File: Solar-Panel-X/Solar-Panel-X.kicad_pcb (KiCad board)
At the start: 6 copper layers, 48.4 x 48.4 mm, 81 parts, among them J1 FTS-105-01-L-DV-A, Q1 BSS138DWQ-7, Q2 MBT2222ADW1T1, Q3 BSS138DWQ-7, Q4 MBT2222ADW1T1, U1 BQ25570RGRR, U2 TSL2561

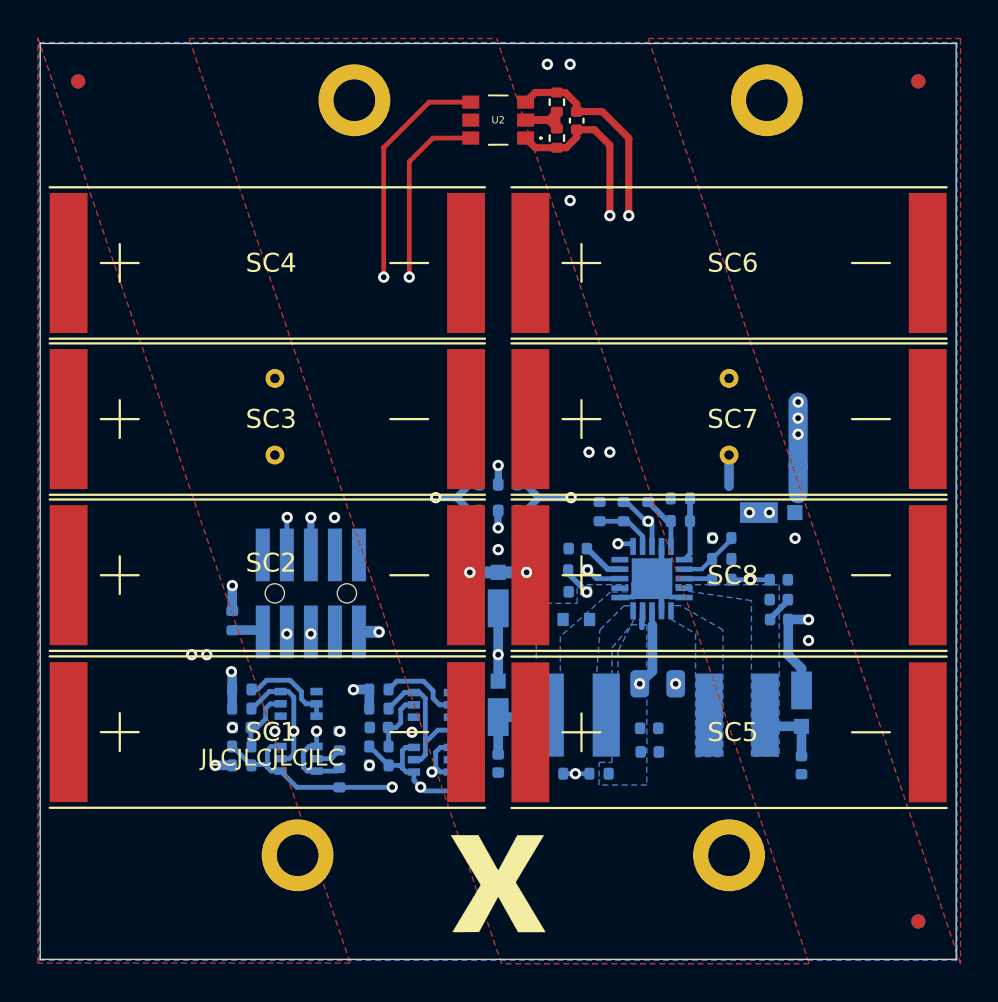
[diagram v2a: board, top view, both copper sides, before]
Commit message: Finish 6 Layer panel versions
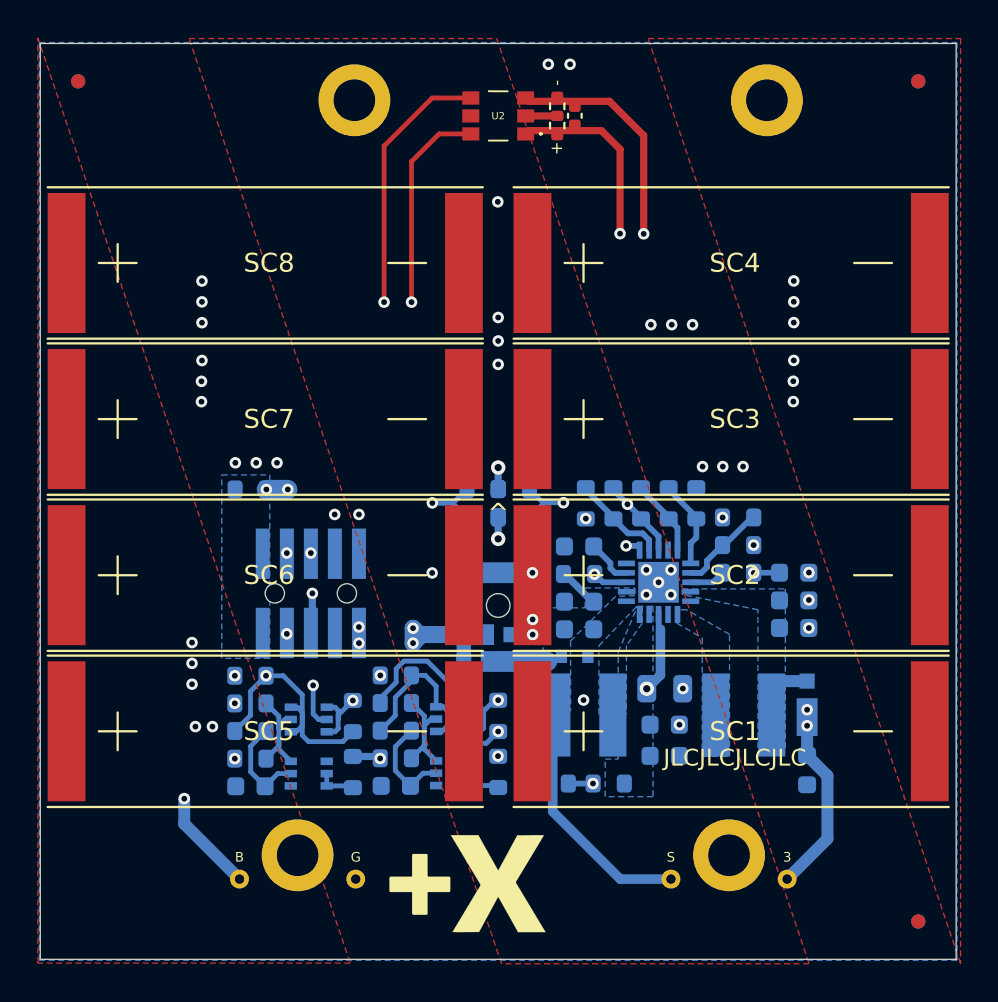
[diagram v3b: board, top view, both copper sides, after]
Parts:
- removed the Ref** at (100.0, 85.1)
- added Ref**: Val**, custom-footprints:pycubed_mini_half, B.Cu at (107.0, 44.5)
- C10, C11, C12, C13, C2, C3, C4, C6, C7, C8, C9: footprint Capacitor_SMD:C_0402_1005Metric -> Capacitor_SMD:C_0603_1608Metric
- J1: footprint batteryboard:FTS-105-XX-YY-DV-A -> solarpanels:SAMTEC-FTS-105-01-X-DV-A
- R10, R11, R12, R13, R16, R17, R18, R3, R5, R6, R7, R8, R9: footprint Resistor_SMD:R_0402_1005Metric -> Resistor_SMD:R_0603_1608Metric
- R14, R15: value 0 -> DNI; footprint Resistor_SMD:R_0402_1005Metric -> Resistor_SMD:R_0603_1608Metric
- R19: renamed from R22; value 0 -> DNI; footprint Resistor_SMD:R_0402_1005Metric -> Resistor_SMD:R_0603_1608Metric
- R20: renamed from R23; value 0 -> DNI; footprint Resistor_SMD:R_0402_1005Metric -> Resistor_SMD:R_0603_1608Metric
- R21: renamed from R20; footprint Resistor_SMD:R_0402_1005Metric -> Resistor_SMD:R_0603_1608Metric
- R22: renamed from R21; footprint Resistor_SMD:R_0402_1005Metric -> Resistor_SMD:R_0603_1608Metric
- R23: renamed from R24; footprint Resistor_SMD:R_0402_1005Metric -> Resistor_SMD:R_0603_1608Metric
- R24: renamed from R25; footprint Resistor_SMD:R_0402_1005Metric -> Resistor_SMD:R_0603_1608Metric
- R25: renamed from R26; footprint Resistor_SMD:R_0402_1005Metric -> Resistor_SMD:R_0603_1608Metric
- R26: renamed from R27; footprint Resistor_SMD:R_0402_1005Metric -> Resistor_SMD:R_0603_1608Metric
- R27: renamed from R28; footprint Resistor_SMD:R_0402_1005Metric -> Resistor_SMD:R_0603_1608Metric
- R28: renamed from R29; footprint Resistor_SMD:R_0402_1005Metric -> Resistor_SMD:R_0603_1608Metric
- R29: renamed from R30; footprint Resistor_SMD:R_0402_1005Metric -> Resistor_SMD:R_0603_1608Metric
- R30: renamed from R31; footprint Resistor_SMD:R_0402_1005Metric -> Resistor_SMD:R_0603_1608Metric
- R4: renamed from R19; footprint Resistor_SMD:R_0402_1005Metric -> Resistor_SMD:R_0603_1608Metric
- moved TP3 37.9 mm to (122.0, 86.5)
- moved TP2 29.9 mm to (99.2, 86.5)
- moved TP1 26.6 mm to (115.8, 86.5)
- moved TP4 22.5 mm to (93.0, 86.5)
- moved SC2 16.5 mm to (108.5, 70.4)
- moved SC4 16.5 mm to (108.5, 53.9)
- moved D3 15.3 mm to (106.1, 70.3), turned to 180 degrees
- moved R27 14.2 mm to (106.7, 80.8), turned to -90 degrees
- moved R21 11.9 mm to (93.6, 77.2), turned to 0 degrees
- moved R29 9.43 mm to (101.3, 75.7)
- moved R20 9.00 mm to (106.7, 77.8)
- moved Q3 9.00 mm to (104.4, 80.9)
- moved C13 8.70 mm to (101.3, 81.5)
- moved R28 8.55 mm to (101.3, 80.1)
- moved Q4 8.48 mm to (104.4, 78.0)
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- renumbered SC5 to SC1, SC6 to SC2, SC7 to SC3, SC8 to SC4, SC1 to SC5, SC2 to SC6, SC3 to SC7, SC4 to SC8
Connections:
- net SCL2 renamed SCL
- net SDA2 renamed SDA
- J1 pad 10: VUSB -> BATT_P
- J1 pad 4: BURN2 -> GND
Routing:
- net VBAT: track 41.5 -> 11.1 mm, vias 2 -> 4
- net GND: track 25.2 -> 12.3 mm, vias 12 -> 44
- net SDA_LS: track 60.1 -> 47.5 mm
- net SCL: track 23.2 -> 12.8 mm
- net Net-(D3-Pad1): track 13.9 -> 3.67 mm, vias 6 -> 3
- net SDA: track 10.3 -> 16.9 mm
- net Net-(Q4-Pad2): track 1.39 -> 8.01 mm
- net SCL_LS: track 56.9 -> 50.3 mm
- net Net-(Q2-Pad2): track 1.42 -> 6.89 mm, vias 0 -> 2
- net VSOLAR: track 22.5 -> 17.2 mm, vias 1 -> 0
- net /VSOLAR_FULL: track 20.1 -> 24.3 mm, vias 3 -> 4
- net Net-(Q3-Pad6): track 9.56 -> 5.62 mm, vias 2 -> 0
- net Net-(Q3-Pad2): track 5.04 -> 1.89 mm
- net Net-(Q1-Pad6): track 8.89 -> 5.99 mm
- net Net-(Q1-Pad2): track 4.82 -> 1.93 mm
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- added copper zone on In3.Cu, net +3V3
- added copper zone on B.Cu, net BATT_P
- added copper zone on In1.Cu, net GND
- added copper zone on In2.Cu, net VBAT
- removed copper zone on In1.Cu, net +3V3
- removed copper zone on In2.Cu, net +3V3
- removed copper zone on In3.Cu, net GND
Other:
- outline, holes or cut-outs redrawn
- board text added: "1.3V3 3.BURN1 5.COIL_P 7.SDA 9.BATT_P"
- board text added: "2.GND 4.GND 6.COIL_N 8.SCL 10.BATT_P"
- board text added: "3"
- board text added: "B"
- board text added: "G"
- board text added: "Rev B2/01"
- board text added: "S"
- board text added: "^"
- board text added: "⊗"
- board text added: "⊙"
- board text removed: "Cable Pinout 1.BATT_P 2.VUSB 3.BURN1 4.BURN2 5.COIL_P 6.COIL_N 7.SDA 8.SCL 9.+3V3 10.GND"
- board text removed: "v04"
